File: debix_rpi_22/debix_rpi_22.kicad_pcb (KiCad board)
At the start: 2 copper layers, 70.4 x 12.5 mm, 2 parts, among them J1 Conn_01x24, J3 RPi 22 Pin MIPI CSI-2

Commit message: FPCB with Siffeners no.w
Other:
- board text added: "Stiffener 0.25x8x11.5mm, 0.3mm total height"
- board text added: "Stiffener 0.25x8x12.5mm, 0.3mm total height"
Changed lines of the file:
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@@
 		(allow_soldermask_bridges_in_footprints no)
 		(tenting front back)
-		(grid_origin 180 140.65)
+		(grid_origin 110 141.65)
 		(pcbplotparams
 			(layerselection 0x00000000_00000000_55555555_5755f5ff)
@@
 	)
 	(gr_line
+		(start 117.8 129.5)
+		(end 117.8 142)
+		(stroke
+			(width 0.1)
+			(type default)
+		)
+		(layer "Eco2.User")
+	)
+	(gr_line
+		(start 180.2 129.5)
+		(end 172.2 129.5)
+		(stroke
+			(width 0.1)
+			(type default)
+		)
+		(layer "Eco2.User")
+	)
+	(gr_line
+		(start 117.8 142)
+		(end 109.8 142)
+		(stroke
+			(width 0.1)
+			(type default)
+		)
+		(layer "Eco2.User")
+	)
+	(gr_line
+		(start 109.8 142)
+		(end 109.8 129.5)
+		(stroke
+			(width 0.1)
+			(type default)
+		)
+		(layer "Eco2.User")
+	)
+	(gr_line
+		(start 180.2 141)
+		(end 172.2 141)
+		(stroke
+			(width 0.1)
+			(type default)
+		)
+		(layer "Eco2.User")
+	)
+	(gr_line
+		(start 109.8 129.5)
+		(end 117.8 129.5)
+		(stroke
+			(width 0.1)
+			(type default)
+		)
+		(layer "Eco2.User")
+	)
+	(gr_line
+		(start 172.2 141)
+		(end 172.2 129.5)
+		(stroke
+			(width 0.1)
+			(type default)
+		)
+		(layer "Eco2.User")
+	)
+	(gr_line
+		(start 180.2 141)
+		(end 180.2 129.5)
+		(stroke
+			(width 0.1)
+			(type default)
+		)
+		(layer "Eco2.User")
+	)
+	(gr_line
 		(start 109.8 142)
 		(end 127.5 142)
@@
 			)
 			(justify left bottom)
+		)
+	)
+	(gr_text "Stiffener 0.25x8x11.5mm, 0.3mm total height"
+		(at 176.5 128.2 90)
+		(layer "Eco2.User")
+		(effects
+			(font
+				(size 1 1)
+				(thickness 0.15)
+			)
+			(justify left bottom)
+		)
+	)
+	(gr_text "Stiffener 0.25x8x12.5mm, 0.3mm total height"
+		(at 114.6 128.25 90)
+		(layer "Eco2.User")
+		(effects
+			(font
+				(size 1 1)
+				(thickness 0.15)
+			)
+			(justify left bottom)

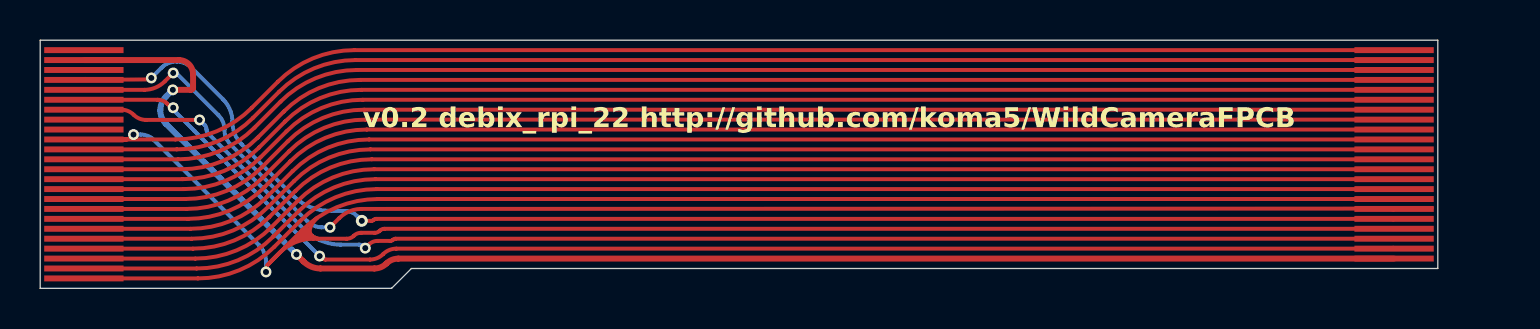
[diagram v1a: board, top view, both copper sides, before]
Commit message: moved silkscreen prepare for v0.3
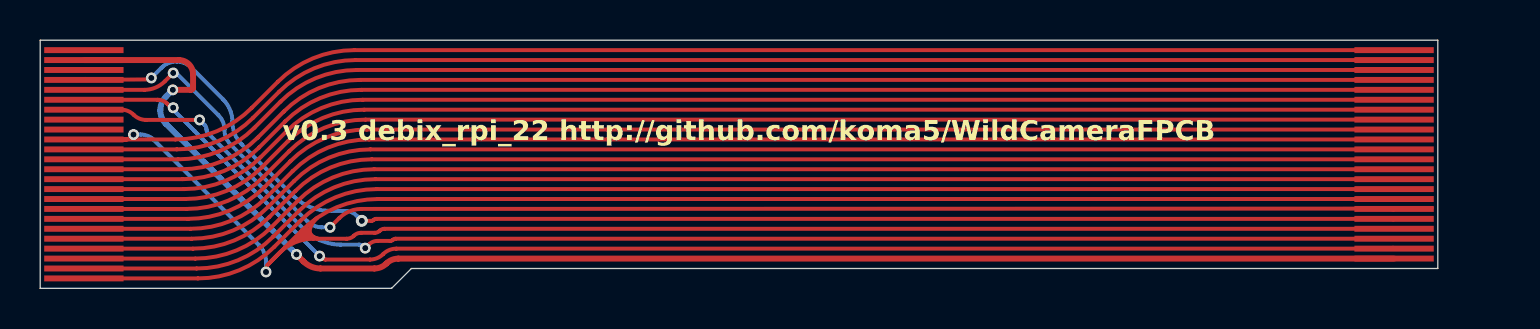
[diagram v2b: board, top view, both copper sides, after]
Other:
- board text added: "v0.3 debix_rpi_22 http://github.com/koma5/WildCameraFPCB"
- board text removed: "v0.2 debix_rpi_22 http://github.com/koma5/WildCameraFPCB"
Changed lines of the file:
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@@
 		(layer "Edge.Cuts")
 	)
-	(gr_text "v0.2 debix_rpi_22 http://github.com/koma5/WildCameraFPCB"
-		(at 126.05 134 0)
+	(gr_text "v0.3 debix_rpi_22 http://github.com/koma5/WildCameraFPCB"
+		(at 122 134.65 0)
 		(layer "F.SilkS")
 		(effects

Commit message: moved everything F.Cu to B.Cu and everything B.Cu to F.Cu manually.
Not sure if this works. It throws some errors in Rules Checker. In theory this is flipped now.
As both sides of the cables were flipped we should be able to flip the connector with switching out Front with Back.
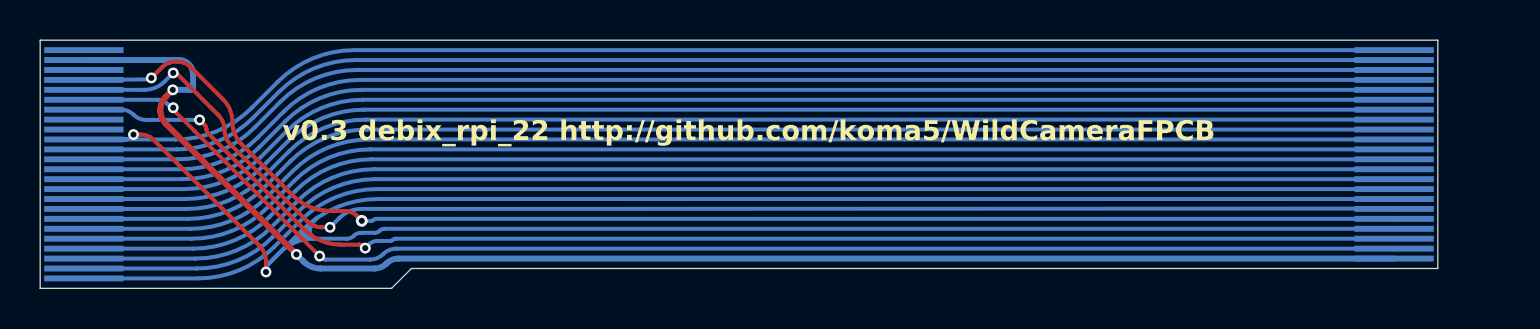
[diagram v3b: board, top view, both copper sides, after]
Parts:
- J1, J3: moved to B.Cu
